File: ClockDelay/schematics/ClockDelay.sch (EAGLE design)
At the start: 72 parts, among them IC1 TL072P, IC2 MEGA168, Q301 2N3904, Q401 2N3904, Q501 2N3904, Q601 2N3904, Q701 2N3904, Y1 16Mhz

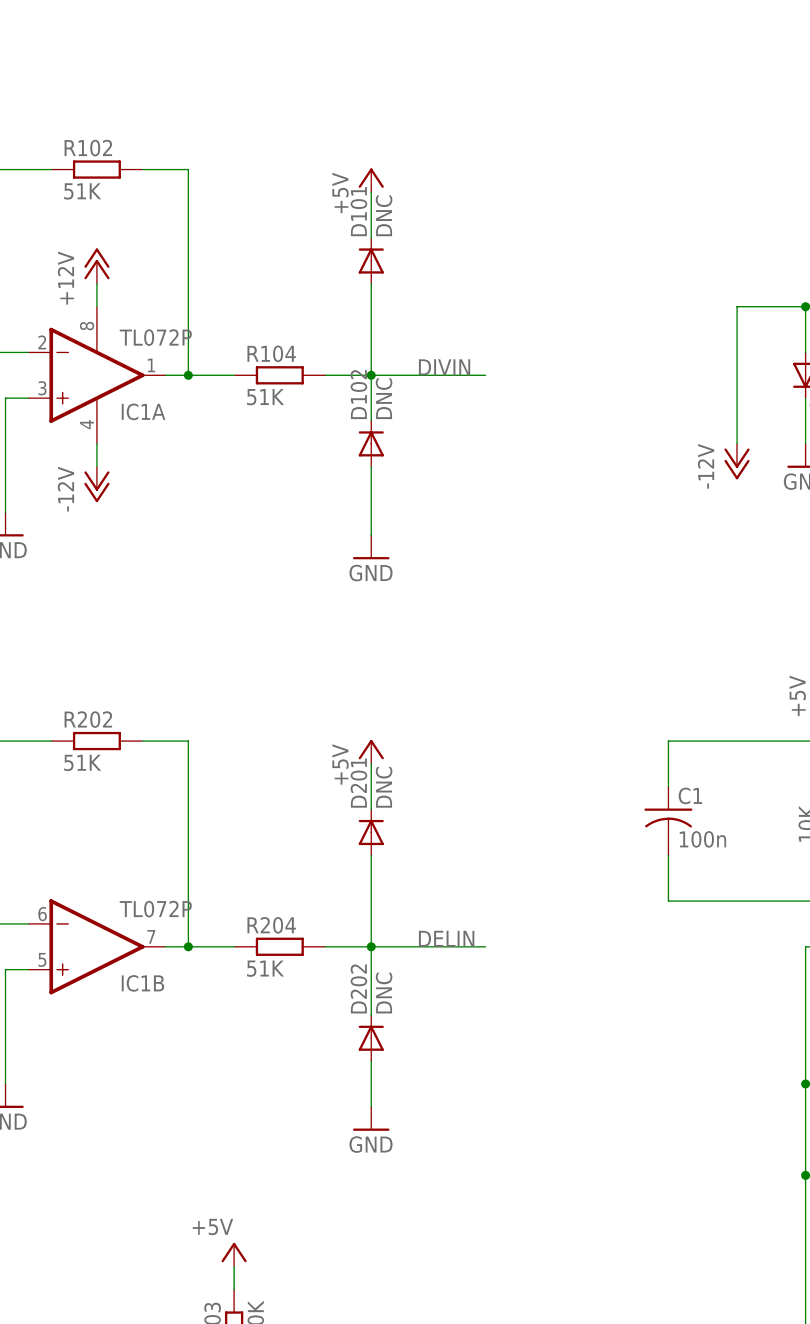
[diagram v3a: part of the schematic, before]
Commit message: removed diodes
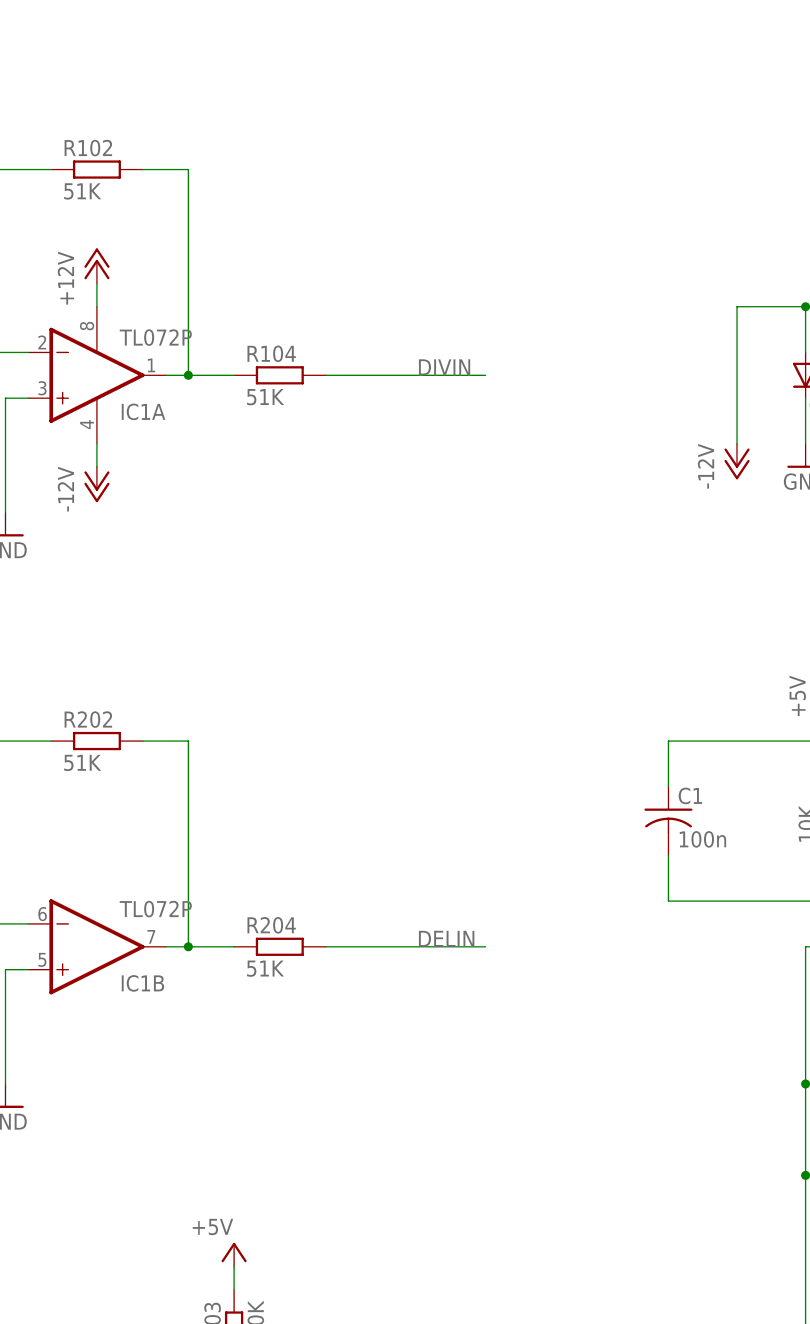
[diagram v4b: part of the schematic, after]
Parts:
- removed D101, D102, D201, D202: DNC, Rebel:DIODE1N4148
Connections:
- net +5V: no longer D101.C, D201.C
- net DELIN: no longer D201.A, D202.C
- net DIVIN: no longer D101.A, D102.C
- net GND: no longer D102.A, D202.A
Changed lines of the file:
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@@
 <?xml version="1.0" encoding="utf-8"?>
 <!DOCTYPE eagle SYSTEM "eagle.dtd">
-<eagle version="6.1">
+<eagle version="6.3">
 <drawing>
 <settings>
@@
 <part name="GND1" library="supply1" deviceset="GND" device=""/>
 <part name="GND4" library="supply1" deviceset="GND" device=""/>
-<part name="D101" library="Rebel" deviceset="DIODE" device="1N4148" value="DNC"/>
 <part name="P+1" library="supply1" deviceset="+12V" device=""/>
-<part name="P+3" library="supply1" deviceset="+5V" device=""/>
 <part name="R202" library="Rebel" deviceset="R-EU_" device="0204/7" value="51K"/>
 <part name="R201" library="Rebel" deviceset="R-EU_" device="0204/7" value="120K"/>
@@
 <part name="GND7" library="supply1" deviceset="GND" device=""/>
 <part name="GND8" library="supply1" deviceset="GND" device=""/>
-<part name="D201" library="Rebel" deviceset="DIODE" device="1N4148" value="DNC"/>
 <part name="P+5" library="supply1" deviceset="+12V" device=""/>
-<part name="P+6" library="supply1" deviceset="+5V" device=""/>
 <part name="CLKIN" library="Rebel" deviceset="CON-LUMBERG_1502_03" device=""/>
 <part name="DELOUT" library="Rebel" deviceset="CON-LUMBERG_1502_03" device=""/>
@@
 <part name="P+11" library="supply1" deviceset="+12V" device=""/>
 <part name="GND29" library="supply1" deviceset="GND" device=""/>
-<part name="D102" library="Rebel" deviceset="DIODE" device="1N4148" value="DNC"/>
-<part name="D202" library="Rebel" deviceset="DIODE" device="1N4148" value="DNC"/>
-<part name="GND30" library="supply1" deviceset="GND" device=""/>
-<part name="GND31" library="supply1" deviceset="GND" device=""/>
 <part name="GND32" library="supply1" deviceset="GND" device=""/>
 <part name="P+12" library="supply1" deviceset="+5V" device=""/>
@@
 <instance part="GND1" gate="1" x="33.02" y="7.62"/>
 <instance part="GND4" gate="1" x="25.4" y="-15.24"/>
-<instance part="D101" gate="G$1" x="101.6" y="10.16" rot="R90"/>
 <instance part="P+1" gate="1" x="33.02" y="38.1"/>
-<instance part="P+3" gate="1" x="101.6" y="20.32"/>
 <instance part="R202" gate="G$1" x="71.12" y="-43.18"/>
 <instance part="R201" gate="G$1" x="48.26" y="-43.18"/>
@@
 <instance part="GND7" gate="1" x="33.02" y="-55.88"/>
 <instance part="GND8" gate="1" x="25.4" y="-78.74"/>
-<instance part="D201" gate="G$1" x="101.6" y="-53.34" rot="R90"/>
 <instance part="P+5" gate="1" x="33.02" y="-25.4"/>
-<instance part="P+6" gate="1" x="101.6" y="-43.18"/>
 <instance part="CLKIN" gate="G$1" x="40.64" y="-121.92" rot="R180"/>
 <instance part="DELOUT" gate="G$1" x="337.82" y="-73.66"/>
@@
 <instance part="P+11" gate="1" x="304.8" y="-106.68"/>
 <instance part="GND29" gate="1" x="55.88" y="-137.16"/>
-<instance part="D102" gate="G$1" x="101.6" y="-10.16" rot="R90"/>
-<instance part="D202" gate="G$1" x="101.6" y="-76.2" rot="R90"/>
-<instance part="GND30" gate="1" x="101.6" y="-22.86"/>
-<instance part="GND31" gate="1" x="101.6" y="-86.36"/>
 <instance part="GND32" gate="1" x="215.9" y="-2.54"/>
 <instance part="P+12" gate="1" x="215.9" y="30.48" smashed="yes">
@@
 </segment>
 <segment>
-<pinref part="GND31" gate="1" pin="GND"/>
-<pinref part="D202" gate="G$1" pin="A"/>
-<wire x1="101.6" y1="-83.82" x2="101.6" y2="-78.74" width="0.1524" layer="91"/>
-</segment>
-<segment>
-<pinref part="GND30" gate="1" pin="GND"/>
-<pinref part="D102" gate="G$1" pin="A"/>
-<wire x1="101.6" y1="-20.32" x2="101.6" y2="-12.7" width="0.1524" layer="91"/>
-</segment>
-<segment>
 <pinref part="D1" gate="G$1" pin="A"/>
 <wire x1="215.9" y1="5.08" x2="215.9" y2="0" width="0.1524" layer="91"/>
@@
 <segment>
 <pinref part="R104" gate="G$1" pin="2"/>
-<wire x1="96.52" y1="-2.54" x2="101.6" y2="-2.54" width="0.1524" layer="91"/>
-<pinref part="D101" gate="G$1" pin="A"/>
-<wire x1="101.6" y1="-2.54" x2="101.6" y2="7.62" width="0.1524" layer="91"/>
-<junction x="101.6" y="-2.54"/>
-<pinref part="D102" gate="G$1" pin="C"/>
-<wire x1="101.6" y1="-7.62" x2="101.6" y2="-2.54" width="0.1524" layer="91"/>
-<wire x1="101.6" y1="-2.54" x2="114.3" y2="-2.54" width="0.1524" layer="91"/>
+<wire x1="96.52" y1="-2.54" x2="114.3" y2="-2.54" width="0.1524" layer="91"/>
 <label x="106.68" y="-2.54" size="1.778" layer="95"/>
 </segment>
@@
 </net>
 <net name="+5V" class="0">
-<segment>
-<pinref part="D101" gate="G$1" pin="C"/>
-<pinref part="P+3" gate="1" pin="+5V"/>
-<wire x1="101.6" y1="17.78" x2="101.6" y2="12.7" width="0.1524" layer="91"/>
-</segment>
-<segment>
-<pinref part="D201" gate="G$1" pin="C"/>
-<pinref part="P+6" gate="1" pin="+5V"/>
-<wire x1="101.6" y1="-45.72" x2="101.6" y2="-50.8" width="0.1524" layer="91"/>
-</segment>
 <segment>
 <pinref part="IC2" gate="G$1" pin="VCC@1"/>
@@
 <segment>
 <pinref part="R204" gate="G$1" pin="2"/>
-<wire x1="96.52" y1="-66.04" x2="101.6" y2="-66.04" width="0.1524" layer="91"/>
-<pinref part="D201" gate="G$1" pin="A"/>
-<wire x1="101.6" y1="-66.04" x2="101.6" y2="-55.88" width="0.1524" layer="91"/>
-<pinref part="D202" gate="G$1" pin="C"/>
-<wire x1="101.6" y1="-73.66" x2="101.6" y2="-66.04" width="0.1524" layer="91"/>
-<junction x="101.6" y="-66.04"/>
-<wire x1="101.6" y1="-66.04" x2="114.3" y2="-66.04" width="0.1524" layer="91"/>
+<wire x1="96.52" y1="-66.04" x2="114.3" y2="-66.04" width="0.1524" layer="91"/>
 <label x="106.68" y="-66.04" size="1.778" layer="95"/>
 </segment>

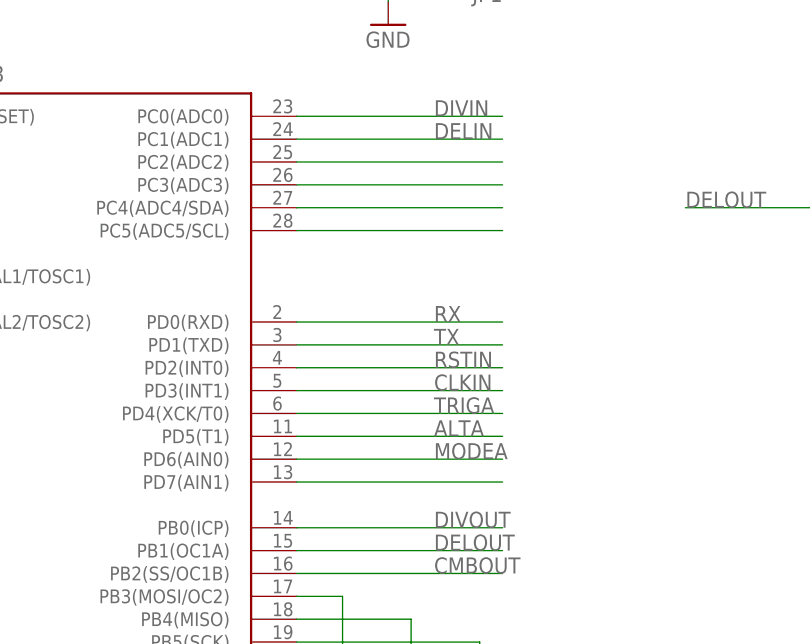
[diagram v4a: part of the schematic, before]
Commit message: removed unused nets and tidied routing, changed rev number to 3
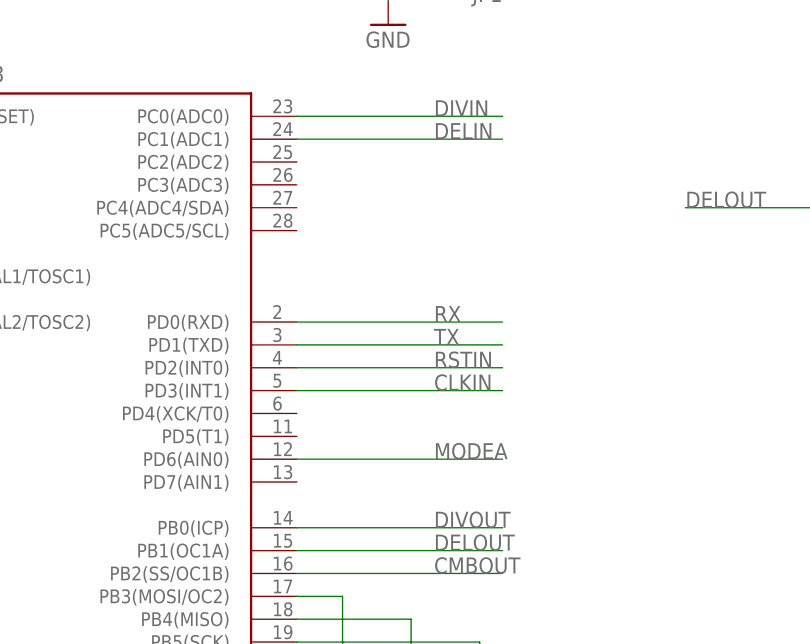
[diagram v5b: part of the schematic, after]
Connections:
- removed net ALTA: IC2.PD5(T1)
- removed net MODEB: IC2.PD7(AIN1)
- removed net N$14: IC2.PC2(ADC2)
- removed net N$15: IC2.PC3(ADC3)
- removed net N$16: IC2.PC4(ADC4/SDA)
- removed net N$17: IC2.PC5(ADC5/SCL)
- removed net TRIGA: IC2.PD4(XCK/T0)
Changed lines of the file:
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@@
 <layer number="106" name="bPlate" color="7" fill="1" visible="yes" active="yes"/>
 <layer number="107" name="Crop" color="7" fill="1" visible="yes" active="yes"/>
+<layer number="108" name="fp8" color="7" fill="1" visible="no" active="yes"/>
+<layer number="109" name="fp9" color="7" fill="1" visible="no" active="yes"/>
+<layer number="110" name="fp0" color="7" fill="1" visible="no" active="yes"/>
+<layer number="111" name="LPC17xx" color="7" fill="1" visible="yes" active="yes"/>
+<layer number="112" name="tSilk" color="7" fill="1" visible="yes" active="yes"/>
 <layer number="116" name="Patch_BOT" color="7" fill="1" visible="yes" active="yes"/>
 <layer number="121" name="_tsilk" color="7" fill="1" visible="yes" active="yes"/>
 <layer number="122" name="_bsilk" color="7" fill="1" visible="yes" active="yes"/>
+<layer number="123" name="tTestmark" color="7" fill="1" visible="no" active="yes"/>
+<layer number="124" name="bTestmark" color="7" fill="1" visible="no" active="yes"/>
 <layer number="125" name="_tNames" color="7" fill="1" visible="yes" active="yes"/>
+<layer number="126" name="_bNames" color="7" fill="1" visible="yes" active="yes"/>
+<layer number="127" name="_tValues" color="7" fill="1" visible="yes" active="yes"/>
+<layer number="128" name="_bValues" color="7" fill="1" visible="yes" active="yes"/>
+<layer number="131" name="tAdjust" color="7" fill="1" visible="no" active="yes"/>
+<layer number="132" name="bAdjust" color="7" fill="1" visible="no" active="yes"/>
 <layer number="144" name="Drill_legend" color="7" fill="1" visible="yes" active="yes"/>
 <layer number="151" name="HeatSink" color="7" fill="1" visible="yes" active="yes"/>
+<layer number="152" name="_bDocu" color="7" fill="1" visible="yes" active="yes"/>
+<layer number="199" name="Contour" color="7" fill="1" visible="yes" active="yes"/>
 <layer number="200" name="200bmp" color="7" fill="1" visible="yes" active="yes"/>
 <layer number="201" name="201bmp" color="7" fill="1" visible="yes" active="yes"/>
@@
 <layer number="223" name="223bmp" color="7" fill="1" visible="yes" active="yes"/>
 <layer number="224" name="224bmp" color="7" fill="1" visible="yes" active="yes"/>
+<layer number="248" name="Housing" color="7" fill="1" visible="yes" active="yes"/>
+<layer number="249" name="Edge" color="7" fill="1" visible="yes" active="yes"/>
 <layer number="250" name="Descript" color="7" fill="1" visible="yes" active="yes"/>
 <layer number="251" name="SMDround" color="7" fill="1" visible="yes" active="yes"/>
@@
 </segment>
 </net>
-<net name="N$14" class="0">
-<segment>
-<pinref part="IC2" gate="G$1" pin="PC2(ADC2)"/>
-<wire x1="218.44" y1="-66.04" x2="241.3" y2="-66.04" width="0.1524" layer="91"/>
-</segment>
-</net>
-<net name="N$15" class="0">
-<segment>
-<pinref part="IC2" gate="G$1" pin="PC3(ADC3)"/>
-<wire x1="218.44" y1="-68.58" x2="241.3" y2="-68.58" width="0.1524" layer="91"/>
-</segment>
-</net>
-<net name="N$16" class="0">
-<segment>
-<pinref part="IC2" gate="G$1" pin="PC4(ADC4/SDA)"/>
-<wire x1="218.44" y1="-71.12" x2="241.3" y2="-71.12" width="0.1524" layer="91"/>
-</segment>
-</net>
-<net name="N$17" class="0">
-<segment>
-<pinref part="IC2" gate="G$1" pin="PC5(ADC5/SCL)"/>
-<wire x1="218.44" y1="-73.66" x2="241.3" y2="-73.66" width="0.1524" layer="91"/>
-</segment>
-</net>
 <net name="N$18" class="0">
 <segment>
@@
 <wire x1="223.52" y1="-114.3" x2="223.52" y2="-121.92" width="0.1524" layer="91"/>
 <pinref part="LED1" gate="G$1" pin="A"/>
-</segment>
-</net>
-<net name="ALTA" class="0">
-<segment>
-<pinref part="IC2" gate="G$1" pin="PD5(T1)"/>
-<wire x1="218.44" y1="-96.52" x2="241.3" y2="-96.52" width="0.1524" layer="91"/>
-<label x="233.68" y="-96.52" size="1.778" layer="95"/>
-</segment>
-</net>
-<net name="TRIGA" class="0">
-<segment>
-<pinref part="IC2" gate="G$1" pin="PD4(XCK/T0)"/>
-<wire x1="218.44" y1="-93.98" x2="241.3" y2="-93.98" width="0.1524" layer="91"/>
-<label x="233.68" y="-93.98" size="1.778" layer="95"/>
 </segment>
 </net>
@@
 </segment>
 </net>
-<net name="MODEB" class="0">
-<segment>
-<pinref part="IC2" gate="G$1" pin="PD7(AIN1)"/>
-<wire x1="218.44" y1="-101.6" x2="241.3" y2="-101.6" width="0.1524" layer="91"/>
-</segment>
-</net>

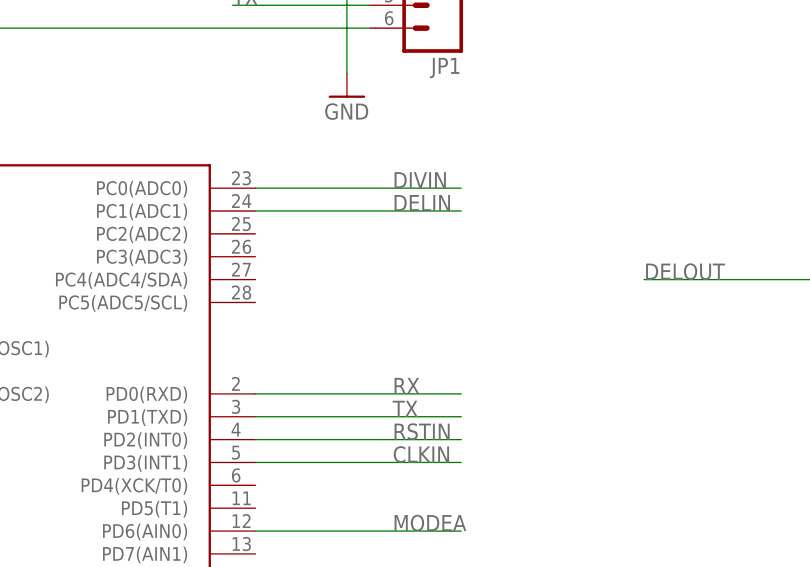
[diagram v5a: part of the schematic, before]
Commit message: added header for unused analogue input pins
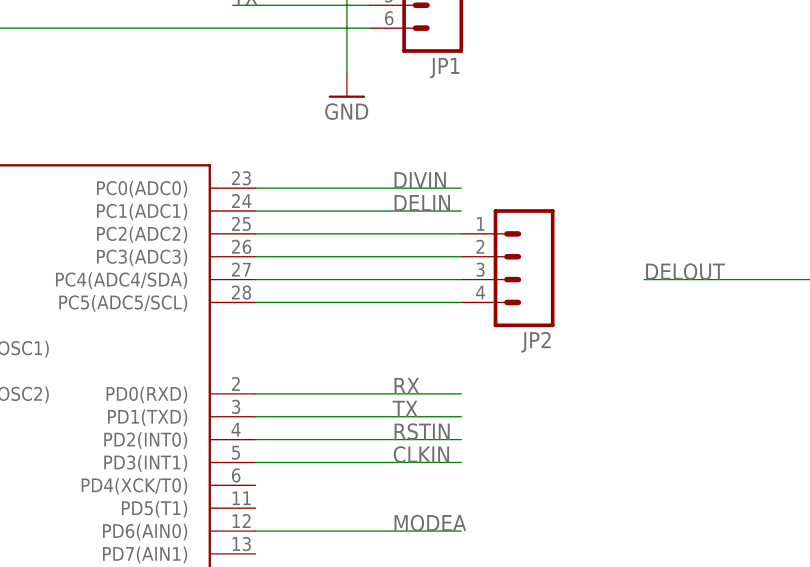
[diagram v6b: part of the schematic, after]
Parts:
- added JP2: (no value), SparkFun:M04PTH
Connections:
- new net N$11: IC2.PC2(ADC2), JP2.1
- new net N$13: IC2.PC3(ADC3), JP2.2
- new net N$14: IC2.PC4(ADC4/SDA), JP2.3
- new net N$15: IC2.PC5(ADC5/SCL), JP2.4
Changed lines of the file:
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@@
 <part name="P-3" library="supply1" deviceset="-12V" device=""/>
 <part name="P-4" library="supply1" deviceset="-12V" device=""/>
+<part name="JP2" library="SparkFun" deviceset="M04" device="PTH"/>
 </parts>
 <sheets>
@@
 <instance part="P-3" gate="1" x="33.02" y="-17.78"/>
 <instance part="P-4" gate="1" x="33.02" y="-81.28"/>
+<instance part="JP2" gate="G$1" x="246.38" y="-68.58" rot="R180"/>
 </instances>
 <busses>
@@
 </segment>
 </net>
+<net name="N$11" class="0">
+<segment>
+<pinref part="IC2" gate="G$1" pin="PC2(ADC2)"/>
+<pinref part="JP2" gate="G$1" pin="1"/>
+<wire x1="241.3" y1="-66.04" x2="218.44" y2="-66.04" width="0.1524" layer="91"/>
+</segment>
+</net>
+<net name="N$13" class="0">
+<segment>
+<pinref part="IC2" gate="G$1" pin="PC3(ADC3)"/>
+<pinref part="JP2" gate="G$1" pin="2"/>
+<wire x1="241.3" y1="-68.58" x2="218.44" y2="-68.58" width="0.1524" layer="91"/>
+</segment>
+</net>
+<net name="N$14" class="0">
+<segment>
+<pinref part="IC2" gate="G$1" pin="PC4(ADC4/SDA)"/>
+<pinref part="JP2" gate="G$1" pin="3"/>
+<wire x1="241.3" y1="-71.12" x2="218.44" y2="-71.12" width="0.1524" layer="91"/>
+</segment>
+</net>
+<net name="N$15" class="0">
+<segment>
+<pinref part="IC2" gate="G$1" pin="PC5(ADC5/SCL)"/>
+<pinref part="JP2" gate="G$1" pin="4"/>
+<wire x1="241.3" y1="-73.66" x2="218.44" y2="-73.66" width="0.1524" layer="91"/>
+</segment>
+</net>
